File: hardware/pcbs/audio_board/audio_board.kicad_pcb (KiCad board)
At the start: 4 copper layers, 152 x 61.5 mm, 160 parts, among them J1 Header_01x04, J2 MTA100_08, J3 NC3MAH, J4 AudioJack3, J5 NC3MAH, J6 NC3FAH1, J7 NC3FAH1, J8 NC3FAH1, J9 AudioJack3, Q1 S8050, Q2 2N7002, Q3 SI2309CDS-T1-GE3, Q4 2N7002, Q5 SI2309CDS-T1-GE3, Q6 2N7002, Q7 SI2309CDS-T1-GE3, U1 Teensy 4.1, U2 LP5907MFX-3.3, U3 LM5158, U4 TAD5242, U5 TAD5242, U6 TAA3040

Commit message: WIP on audio board revg schematics
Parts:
- J1: value Header_01x04 -> Conn_02x06_Odd_Even; footprint conn:PinHeader_1x04_P2.54mm_Vertical -> conn:PinHeader_2x06_P2.54mm_Vertical
- moved J1 5.80 mm to (123.5, 114.3)
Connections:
- J1 pad 1: GND -> /I2S1_RX2
- J1 pad 2: /SDA -> +3.3V
- J1 pad 3: /SCL -> /I2S1_RX1
- J1 pad 4: +3.3V -> /SDA
- U1 pad 14: unconnected-(U1-Pad14) -> /SPDIF_OUT
- U1 pad 15: unconnected-(U1-Pad15) -> /SPDIF_IN
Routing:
- net /I2S1_MCLK: track 0.00 -> 32.2 mm
- net /I2S1_LRCLK: track 184.8 -> 214.2 mm
- net /I2S1_BCLK: track 174.3 -> 202.6 mm
- net /SPDIF_IN: track 0.00 -> 22.6 mm
- net /SPDIF_OUT: track 0.00 -> 22.0 mm
- net +5V: track 79.3 -> 98.7 mm, vias 3 -> 5
- net /SDA: track 28.9 -> 21.5 mm
- net /SCL: track 29.2 -> 26.2 mm
- net +3.3V: track 303.5 -> 301.9 mm
- net GND: vias 256 -> 254

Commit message: prepare for clock fanout
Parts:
- added C57: 1μF, Capacitor_SMD:C_0805_2012Metric, F.Cu at (111.9, 71.5)
- added C58: 1μF, Capacitor_SMD:C_0805_2012Metric, F.Cu at (111.9, 74.5)
- added C59: 1μF, Capacitor_SMD:C_0805_2012Metric, F.Cu at (111.9, 77.5)
- added FB1: FerriteBead_Small, Inductor_SMD:L_0805_2012Metric, F.Cu at (98.7, 76.9)
- added R10: 47Ω, Resistor_SMD:R_0805_2012Metric, F.Cu at (92.2, 77.0)
- added R11: 47Ω, Resistor_SMD:R_0805_2012Metric, F.Cu at (92.2, 80.0)
- added R12: 47Ω, Resistor_SMD:R_0805_2012Metric, F.Cu at (92.2, 82.9)
- added R2: 47Ω, Resistor_SMD:R_0805_2012Metric, F.Cu at (92.2, 62.3)
- added R3: 47Ω, Resistor_SMD:R_0805_2012Metric, F.Cu at (92.2, 65.2)
- added R33: 10Ω, Resistor_SMD:R_0805_2012Metric, F.Cu at (111.4, 82.5)
- added R4: 47Ω, Resistor_SMD:R_0805_2012Metric, F.Cu at (92.2, 68.2)
- added R45: 10Ω, Resistor_SMD:R_0805_2012Metric, F.Cu at (105.0, 82.5)
- added R5: 47Ω, Resistor_SMD:R_0805_2012Metric, F.Cu at (92.2, 71.1)
- added R57: 10Ω, Resistor_SMD:R_0805_2012Metric, F.Cu at (98.6, 82.5)
- added R6: 47Ω, Resistor_SMD:R_0805_2012Metric, F.Cu at (92.2, 74.1)
- added R63: 10kΩ, Resistor_SMD:R_0805_2012Metric, F.Cu at (98.6, 62.3)
- added R64: 10kΩ, Resistor_SMD:R_0805_2012Metric, F.Cu at (98.6, 65.2)
- added R65: 0Ω, Resistor_SMD:R_0805_2012Metric, F.Cu at (98.6, 68.2)
- added R66: 0Ω, Resistor_SMD:R_0805_2012Metric, F.Cu at (98.6, 71.1)
- added R67: 0Ω, Resistor_SMD:R_0805_2012Metric, F.Cu at (98.6, 74.1)
- added R68: 0Ω, Resistor_SMD:R_0805_2012Metric, F.Cu at (103.0, 62.3)
- added R69: 0Ω, Resistor_SMD:R_0805_2012Metric, F.Cu at (103.0, 65.2)
- added R70: 0Ω, Resistor_SMD:R_0805_2012Metric, F.Cu at (103.0, 68.2)
- added R71: 47Ω, Resistor_SMD:R_0805_2012Metric, F.Cu at (103.0, 71.1)
- added R72: 47Ω, Resistor_SMD:R_0805_2012Metric, F.Cu at (103.0, 74.1)
- added R73: 47Ω, Resistor_SMD:R_0805_2012Metric, F.Cu at (107.4, 62.3)
- added R74: 47Ω, Resistor_SMD:R_0805_2012Metric, F.Cu at (107.4, 65.2)
- added R75: 47Ω, Resistor_SMD:R_0805_2012Metric, F.Cu at (107.4, 68.2)
- added R76: 47Ω, Resistor_SMD:R_0805_2012Metric, F.Cu at (107.4, 71.1)
- added U7: LMK1C1103A, Package_SO:TSSOP-8_4.4x3mm_P0.65mm, F.Cu at (114.0, 63.1)
- added U8: LMK1C1103A, Package_SO:TSSOP-8_4.4x3mm_P0.65mm, F.Cu at (114.0, 67.7)
- R34: renamed from R26; value 2.2kΩ -> 10Ω
- R46: renamed from R38; value 2.2kΩ -> 10Ω
- R58: renamed from R50; value 2.2kΩ -> 10Ω
- renumbered C57 to C60, C58 to C61, C59 to C62, R5 to R13, R6 to R14, R7 to R15, R8 to R16, R9 to R17, R10 to R18, R11 to R19, R12 to R20, R13 to R21, R14 to R22, R15 to R23, R16 to R24, R17 to R25, R18 to R26, R19 to R27, R20 to R28, R21 to R29, R22 to R30, R23 to R31, R24 to R32, R27 to R35, R28 to R36, R29 to R37, R30 to R38, R31 to R39, R32 to R40, R33 to R41, R34 to R42, R35 to R43, R36 to R44, R39 to R47, R40 to R48, R41 to R49, R42 to R50, R43 to R51, R44 to R52, R45 to R53, R46 to R54, R47 to R55, R48 to R56, R51 to R59, R52 to R60, R53 to R61, R54 to R62, R2 to R7, R55 to R77, R56 to R78, R57 to R79, R3 to R8, R58 to R80, R4 to R9
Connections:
- J1 pad 1: /I2S1_RX2 -> GND
- J1 pad 11: +5V -> +3.3V
- J1 pad 2: +3.3V -> +5V
- J1 pad 3: /I2S1_RX1 -> /I2S1_IO2
- J1 pad 5: /I2S1_LRCLK -> /I2S1_IO1
- J1 pad 7: /I2S1_BCLK -> /I2S1_LRCLK
- J1 pad 9: /I2S1_MCLK -> /I2S1_BCLK
- U1 pad 20: /I2S1_LRCLK -> Net-(R11-Pad2)
- U1 pad 21: /I2S1_BCLK -> Net-(R10-Pad2)
- U1 pad 3: /I2S2_FS -> Net-(R2-Pad1)
- U1 pad 4: /I2S2_BCLK -> Net-(R3-Pad1)
- U1 pad 6: /I2S1_RX2 -> Net-(R4-Pad1)
- U1 pad 7: /I2S1_TX1 -> Net-(R5-Pad1)
- U1 pad 8: /I2S1_RX1 -> Net-(R6-Pad1)
- U4 pad 2: /I2S1_BCLK -> /Clock fanout/BCLK1
- U4 pad 3: /I2S1_LRCLK -> /Clock fanout/LRCLK1
- U5 pad 2: /I2S1_BCLK -> /Clock fanout/BCLK2
- U5 pad 3: /I2S1_LRCLK -> /Clock fanout/LRCLK2
- U6 pad 21: /I2S2_RX -> /ADC/DOUT

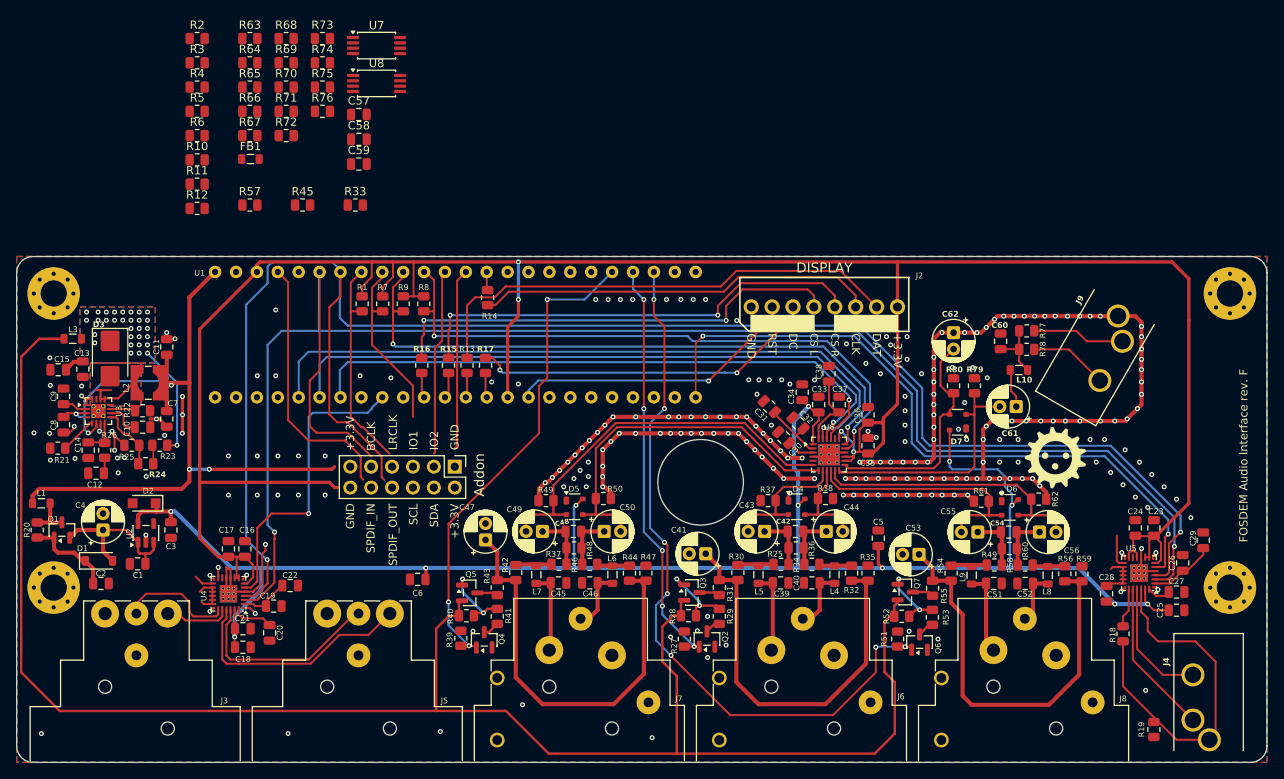
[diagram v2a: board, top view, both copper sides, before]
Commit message: audioboard: route clock fanout
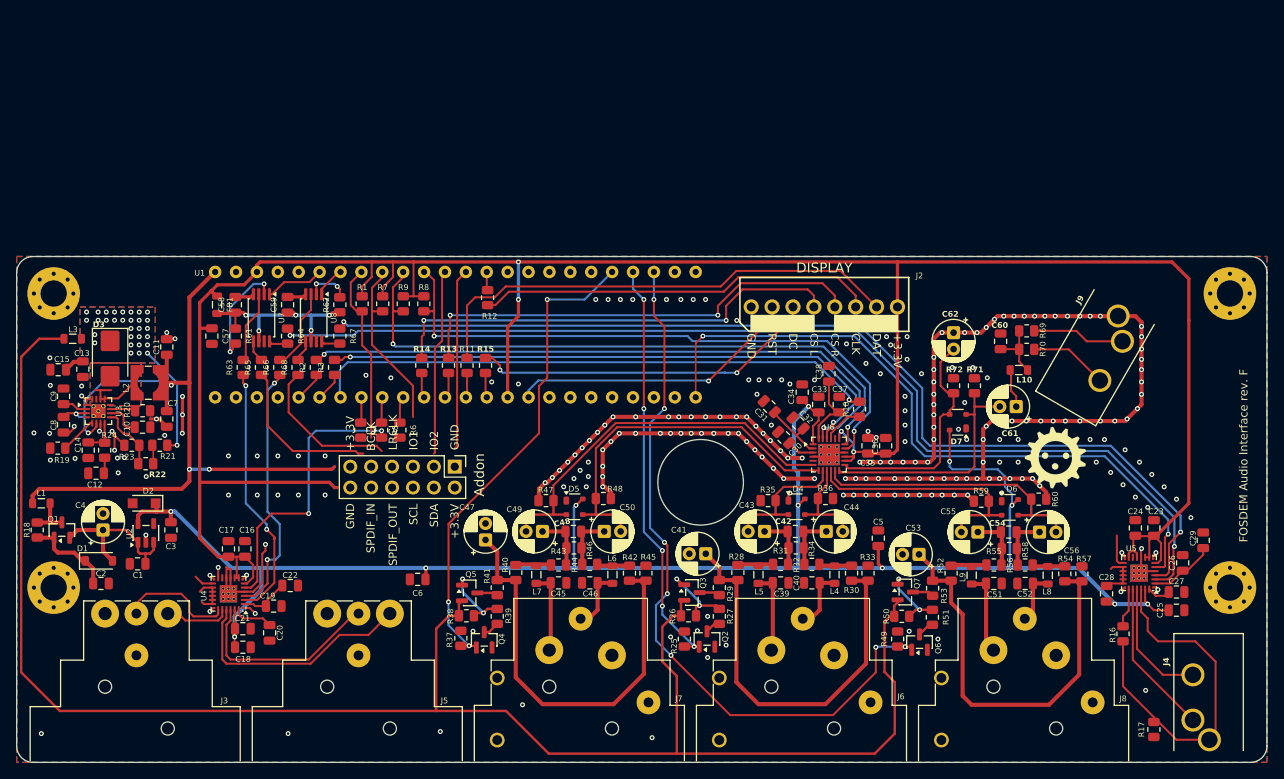
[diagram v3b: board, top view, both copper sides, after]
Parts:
- removed the R10 at (92.2, 77.0)
- removed the R11 at (92.2, 80.0)
- removed the R25 at (163.2, 126.2)
- removed the R37 at (136.2, 126.2)
- removed the R49 at (189.1, 126.2)
- removed the R65 at (98.6, 68.2)
- removed the R66 at (98.6, 71.1)
- removed the R67 at (98.6, 74.1)
- removed the R68 at (103.0, 62.3)
- removed the R69 at (103.0, 65.2)
- removed the R70 at (103.0, 68.2)
- moved R55 100.5 mm to (189.1, 126.2)
- moved R10 84.1 mm to (172.7, 107.3), turned to 90 degrees
- moved R31 67.7 mm to (163.1, 126.2)
- moved R43 53.7 mm to (136.1, 126.2)
- moved R4 46.2 mm to (112.1, 109.9), turned to -90 degrees
- moved R5 44.8 mm to (114.6, 109.9), turned to -90 degrees
- moved R6 43.5 mm to (116.8, 109.9), turned to -90 degrees
- moved R2 42.5 mm to (106.7, 102.2), turned to 90 degrees
- moved R65 40.7 mm to (100.0, 102.2), turned to 90 degrees
- moved R3 40.6 mm to (108.9, 102.2), turned to 90 degrees
- moved R66 37.4 mm to (102.2, 102.2), turned to 90 degrees
- moved R61 36.2 mm to (96.8, 98.4), turned to -90 degrees
- moved U7 35.9 mm to (100.0, 96.2), turned to -90 degrees
- moved C57 32.3 mm to (94.0, 98.4), turned to -90 degrees
- moved R63 31.6 mm to (97.8, 102.2), turned to 90 degrees
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- renumbered R12 to R10, R13 to R11, R14 to R12, R15 to R13, R16 to R14, R17 to R15, R18 to R16, R19 to R17, R20 to R18, R21 to R19, R22 to R20, R23 to R21, R24 to R22, R25 to R23, R26 to R24, R27 to R25, R28 to R26, R29 to R27, R30 to R28, R31 to R29, R32 to R30, R33 to R31, R34 to R32, R35 to R33, R36 to R34, R37 to R35, R38 to R36, R39 to R37, R40 to R38, R41 to R39, R42 to R40, R43 to R41, R44 to R42, R45 to R43, R46 to R44, R47 to R45, R48 to R46, R49 to R47, R50 to R48, R51 to R49, R52 to R50, R53 to R51, R54 to R52, R55 to R53, R56 to R54, R57 to R55, R58 to R56, R59 to R57, R60 to R58, R61 to R59, R62 to R60, R63 to R61, R64 to R62, R71 to R63, R72 to R64, R73 to R65, R74 to R66, R75 to R67, R76 to R68, R77 to R69, R78 to R70, R79 to R71, R80 to R72
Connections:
- net Net-(U7-VDD) renamed /Clock fanout/CVDD
- U1 pad 20: Net-(R11-Pad2) -> /Clock fanout/LRCLK
- U1 pad 21: Net-(R10-Pad2) -> /Clock fanout/BCLK
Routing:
- net /I2S1_LRCLK: track 214.2 -> 18.3 mm, vias 2 -> 0
- net /I2S1_BCLK: track 202.6 -> 19.5 mm, vias 2 -> 0
- net /Clock fanout/BCLK2: track 0.00 -> 131.1 mm, vias 0 -> 2
- net /Clock fanout/LRCLK2: track 0.00 -> 125.4 mm, vias 0 -> 2
- net /I2S1_MCLK: track 32.2 -> 0.00 mm
- net /Clock fanout/LRCLK1: track 0.00 -> 31.4 mm, vias 0 -> 2
- net /Clock fanout/BCLK1: track 0.00 -> 31.4 mm, vias 0 -> 2
- net /Clock fanout/CVDD: track 0.00 -> 24.7 mm, vias 0 -> 5
- net Net-(U7-1G): track 0.00 -> 13.1 mm, vias 0 -> 2
- net Net-(U8-Y0): track 0.00 -> 9.90 mm
- net Net-(U7-Y0): track 0.00 -> 8.77 mm
- net /Clock fanout/BCLK: track 0.00 -> 7.86 mm
- net /I2S2_FS: track 83.7 -> 77.1 mm, vias 1 -> 2
- net /I2S2_BCLK: track 78.5 -> 72.5 mm, vias 1 -> 2
- net Net-(U8-1G): track 0.00 -> 5.38 mm, vias 0 -> 2
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
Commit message: audioboard: finalise routing
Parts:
- added R7: 47Ω, Resistor_SMD:R_0805_2012Metric, F.Cu at (119.7, 109.9)
- added R8: 47Ω, Resistor_SMD:R_0805_2012Metric, F.Cu at (153.0, 101.9)
- J1: value Conn_02x06_Odd_Even -> Conn_02x07_Odd_Even; footprint conn:PinHeader_2x06_P2.54mm_Vertical -> conn:PinHeader_2x07_P2.54mm_Vertical
- moved R16 31.3 mm to (150.8, 102.0)
- moved J1 2.54 mm to (121.0, 114.3)
- moved R6 0.32 mm to (117.2, 109.9)
- renumbered R8 to R10, R9 to R11, R10 to R12, R11 to R13, R12 to R14, R13 to R15, R14 to R16, R15 to R17, R16 to R18, R17 to R19, R18 to R20, R19 to R21, R20 to R22, R21 to R23, R22 to R24, R23 to R25, R24 to R26, R25 to R27, R26 to R28, R27 to R29, R28 to R30, R29 to R31, R30 to R32, R31 to R33, R32 to R34, R33 to R35, R34 to R36, R35 to R37, R36 to R38, R37 to R39, R38 to R40, R39 to R41, R40 to R42, R41 to R43, R42 to R44, R43 to R45, R44 to R46, R45 to R47, R46 to R48, R47 to R49, R48 to R50, R49 to R51, R50 to R52, R51 to R53, R52 to R54, R53 to R55, R54 to R56, R55 to R57, R56 to R58, R57 to R59, R58 to R60, R59 to R61, R60 to R62, R61 to R63, R62 to R64, R63 to R65, R64 to R66, R65 to R67, R66 to R68, R67 to R69, R68 to R70, R69 to R71, R70 to R72, R71 to R73, R72 to R74, R7 to R9
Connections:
- net /CS_RIGHT renamed Net-(R15-Pad1)
- net /DC renamed Net-(R17-Pad1)
- net /I2S1_IO1 renamed Net-(J1-Pin_5)
- net /MOSI renamed Net-(R13-Pad1)
- net /RESET renamed /DISP_RST
- net /SCK renamed Net-(R14-Pad1)
- net Net-(J2-Pin_3) renamed /DISP_DC
- net Net-(J2-Pin_4) renamed /DISP_CS_LEFT
- net Net-(J2-Pin_5) renamed /DISP_CS_RIGHT
- net Net-(J2-Pin_6) renamed /DISP_SCK
- net Net-(J2-Pin_7) renamed /DISP_MOSI
- net Net-(R4-Pad1) renamed /I2S1_RX1
- net Net-(R6-Pad1) renamed /I2S1_RX2
- J1 pad 10: /SPDIF_IN -> /SCL
- J1 pad 11: +3.3V -> /I2S1_BCLK
- J1 pad 12: GND -> +5V
- J1 pad 2: +5V -> GND
- J1 pad 3: /I2S1_IO2 -> /I2S1_TX3
- J1 pad 4: /SDA -> /SPDIF_IN
- J1 pad 6: /SCL -> /SPDIF_OUT
- J1 pad 7: /I2S1_LRCLK -> Net-(J1-Pin_7)
- J1 pad 8: /SPDIF_OUT -> /SDA
- J1 pad 9: /I2S1_BCLK -> /I2S1_LRCLK
- R16 pad 1: /CS_LEFT -> Net-(R16-Pad1)
- R4 pad 2: /I2S1_IO2 -> Net-(J1-Pin_7)
- U1 pad 31: unconnected-(U1-Pad31) -> Net-(R16-Pad1)
- U1 pad 32: /I2S1_TX2 -> Net-(R8-Pad1)
- U1 pad 9: /CS_LEFT -> Net-(R7-Pad1)
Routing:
- net /DISP_CS_LEFT: track 56.4 -> 24.1 mm, vias 2 -> 0
- net /SPDIF_OUT: track 22.0 -> 36.9 mm
- net /SDA: track 21.5 -> 33.5 mm
- net /SCL: track 22.2 -> 32.6 mm
- net /SPDIF_IN: track 22.6 -> 27.8 mm
- net /I2S1_TX2: track 84.2 -> 79.3 mm
- net /I2S1_TX3: track 0.00 -> 4.06 mm
- net Net-(J1-Pin_7): track 0.00 -> 4.06 mm
- net Net-(J1-Pin_5): track 0.00 -> 4.06 mm
- net Net-(R7-Pad1): track 0.00 -> 3.50 mm
- net GND: track 279.5 -> 282.9 mm, vias 251 -> 285
- net Net-(R16-Pad1): track 0.00 -> 3.19 mm
- net Net-(R8-Pad1): track 0.00 -> 3.14 mm
- net /CS_LEFT: track 3.07 -> 0.00 mm
- net +5V: track 98.7 -> 101.2 mm
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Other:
- board text added: "FOSDEM Audio Interface rev. G"
